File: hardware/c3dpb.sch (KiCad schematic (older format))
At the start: 93 parts, among them J1 Conn_01x01, J10 Conn_01x01, J104 Conn_01x01, J11 Conn_01x01, J12 Conn_01x01, J13 Conn_01x01, J14 Conn_01x01, J15 Conn_01x01, J16 Conn_01x01, J17 Conn_01x01, J18 Conn_01x01, J19 Conn_01x01, J2 Conn_01x01, J20 Conn_01x01, J21 Conn_01x01, J22 Conn_01x01, J23 Conn_01x01, J24 Conn_01x01, J25 Conn_01x01, J26 Conn_01x01, J27 Conn_01x01, J28 Conn_01x01, J29 Conn_01x01, J3 Conn_01x01, J30 Conn_01x01, J31 Conn_01x01, J32 Conn_01x01, J33 Conn_01x01, J34 Conn_01x01, J35 Conn_01x01, J36 Conn_01x01, J37 Conn_01x01, J38 Conn_01x01, J4 Conn_01x01, J5 Conn_01x01, J52 Conn_01x01, J6 Conn_01x01, J7 Conn_01x01, J75 Conn_01x01, J76 Conn_01x01, J77 Conn_01x01, J78 Conn_01x01, J8 Conn_01x01, J9 Conn_01x01, SW1 3x6mm, SW2 3x6mm, U1 LPC1769FBD100, X1 12MHz

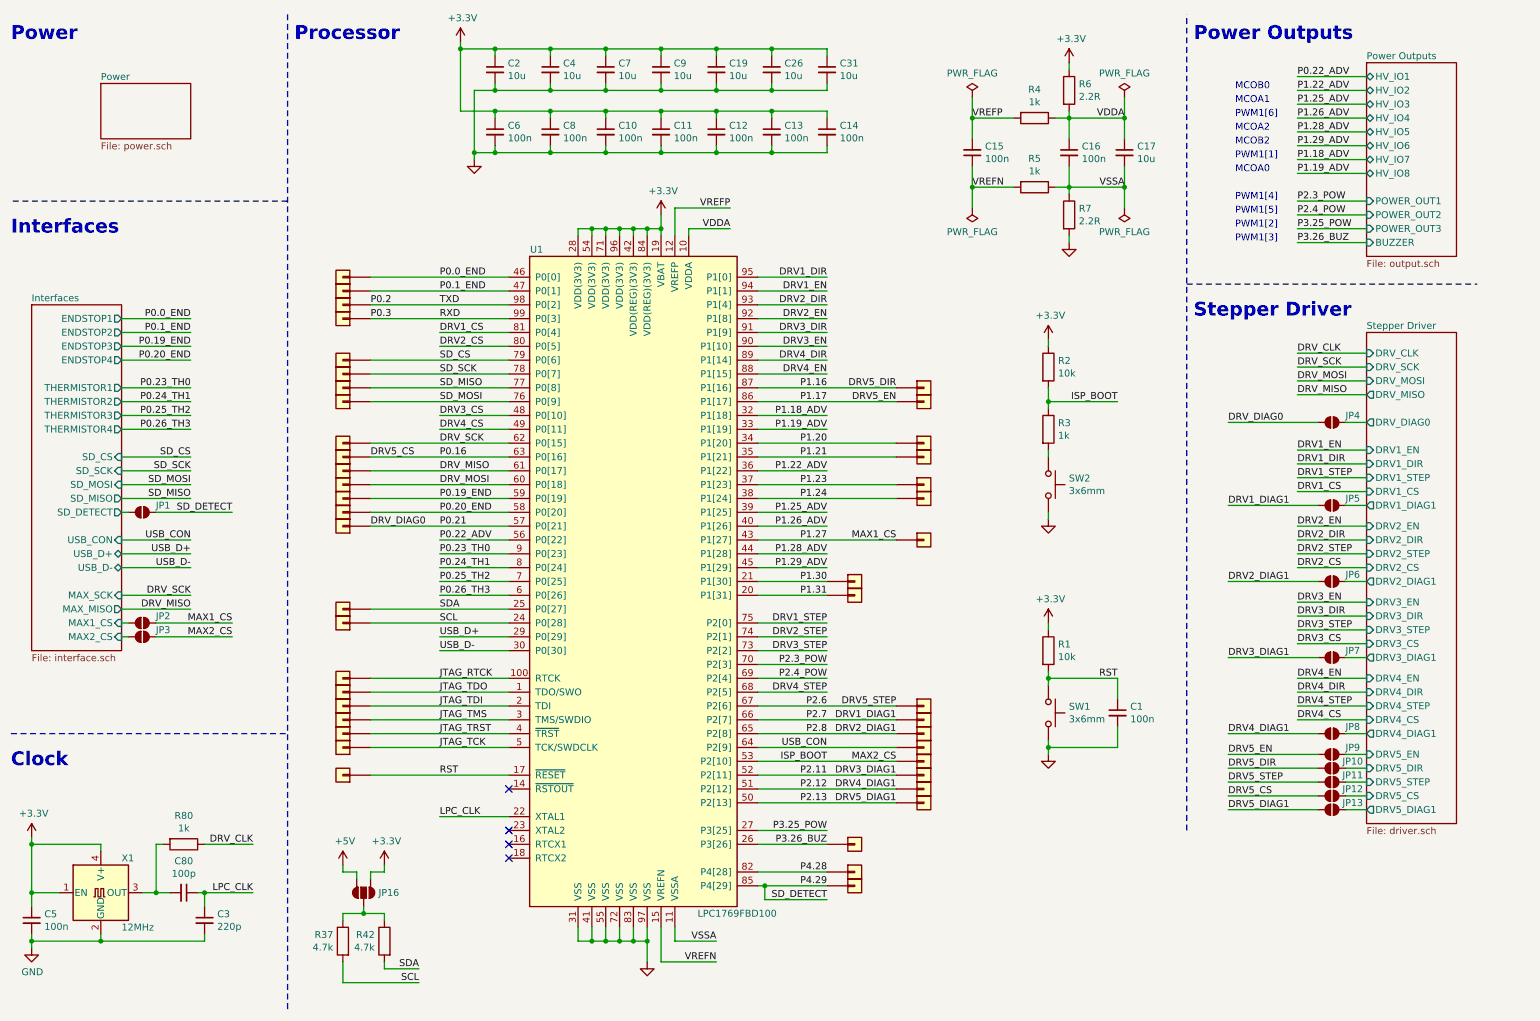
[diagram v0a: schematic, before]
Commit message: replaced stepper driver
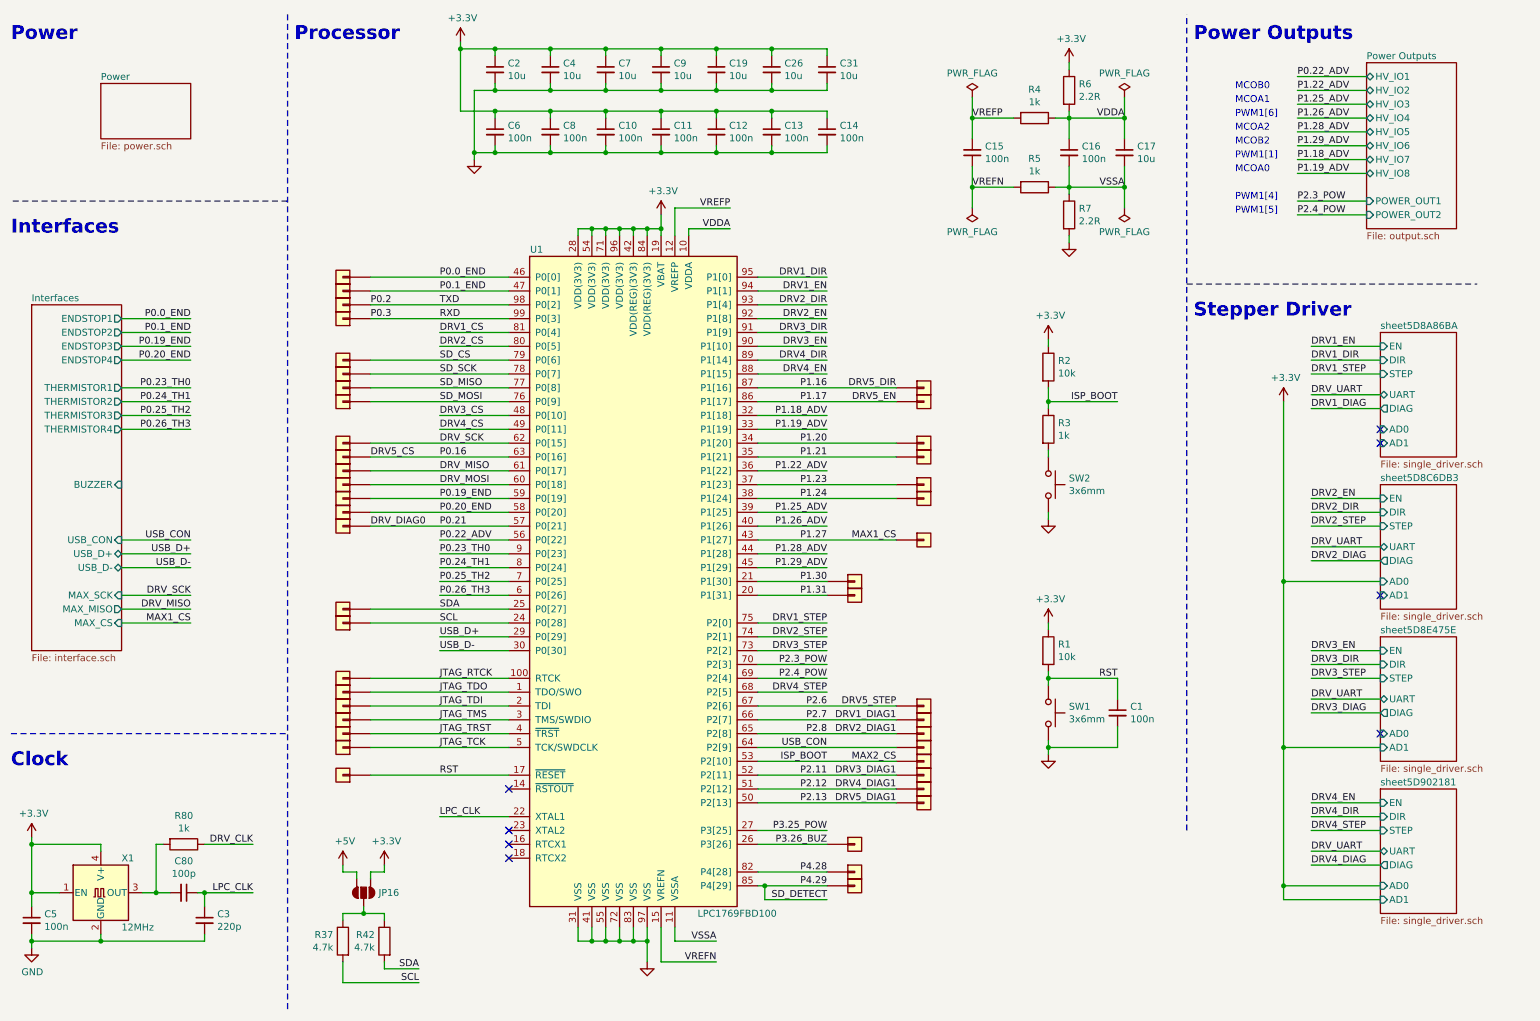
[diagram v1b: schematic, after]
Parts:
- removed JP1, JP10, JP11, JP12, JP13, JP2, JP3, JP4, JP5, JP6, JP7, JP8, JP9: SolderJumper_2_Open, _Generic:Solder Jumper 2P, symbol #PCB_Only:SolderJumper_2_Open
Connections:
- no-connect marks 4 -> 8
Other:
- note removed: "PWM1[2]"
- note removed: "PWM1[3]"
